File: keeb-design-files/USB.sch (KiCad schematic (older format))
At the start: 1 part

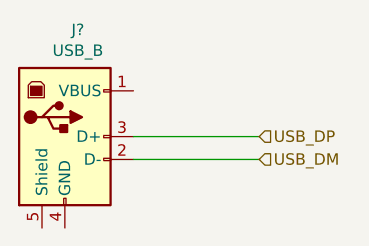
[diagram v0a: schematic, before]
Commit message: Add new Crystal and match symbols and footprints for switches and diodes
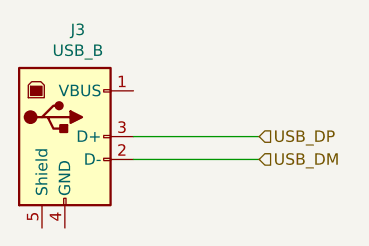
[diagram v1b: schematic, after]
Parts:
- gave numbers to parts that had none: 1
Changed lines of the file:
@@
 $Descr A4 11693 8268
 encoding utf-8
-Sheet 4 6
+Sheet 4 5
 Title "USB and Power Management"
 Date "2020-05-06"
@@
 $EndDescr
 $Comp
-L Connector:USB_B J?
+L Connector:USB_B J3
 U 1 1 5F00EB91
 P 1500 1950
-F 0 "J?" H 1557 2417 50  0000 C CNN
+F 0 "J3" H 1557 2417 50  0000 C CNN
 F 1 "USB_B" H 1557 2326 50  0000 C CNN
 F 2 "" H 1650 1900 50  0001 C CNN

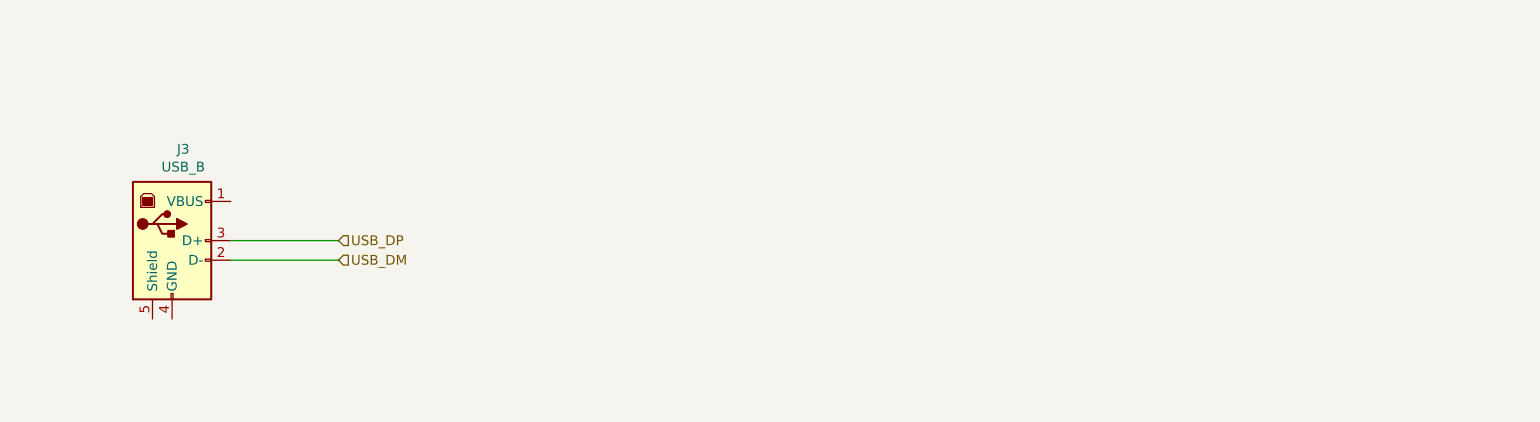
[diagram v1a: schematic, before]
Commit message: Add ESD diodes, USB isolator and LDO to schematic
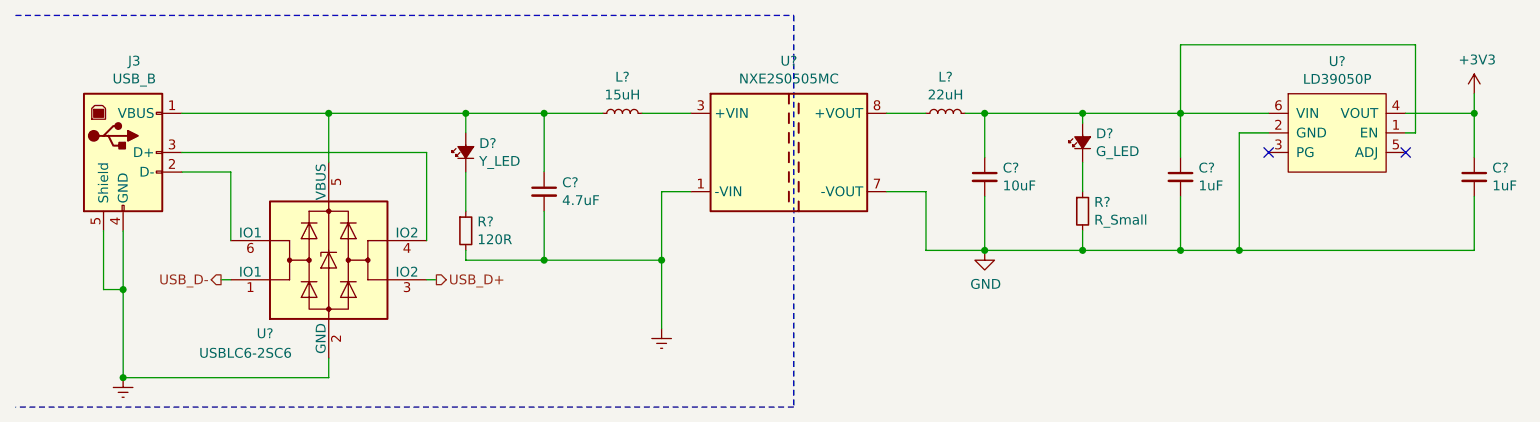
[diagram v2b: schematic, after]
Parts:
- added C?: 4.7uF, symbol Device:C_Small
- added C?: 10uF, symbol Device:C_Small
- added C? (x2): 1uF, symbol Device:C_Small
- added D?: Y_LED, symbol Device:LED_Small_ALT
- added D?: G_LED, symbol Device:LED_Small_ALT
- added L?: 15uH, symbol Device:L_Small
- added L?: 22uH, symbol Device:L_Small
- added R?: 120R, symbol Device:R_Small
- added R?: R_Small, symbol Device:R_Small
- added U?: NXE2S0505MC, Converter_DCDC:Converter_DCDC_muRata_NXE2SxxxxMC_THT, symbol Regulator_Switching:NXE2S0505MC
- added U?: USBLC6-2SC6, Package_TO_SOT_SMD:SOT-23-6, symbol Power_Protection:USBLC6-2SC6
- added U?: LD39050P, Package_DFN_QFN:DFN-6-1EP_3x3mm_P0.95mm_EP1.7x2.6mm, symbol LDO:LD39050P
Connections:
- net at J3.1 (VBUS): now also C?.1, D?.2 (A), L?.1, U?.5 (VBUS)
- net Earth: now reaches J3.4 (GND)
- net Earth: now also J3.5 (Shield), C?.2, R?.2, U?.1 (-VIN), U?.2 (GND)
- net USB_DM: no longer names the net of J3.2 (D-)
- net USB_DM: now also U?.6 (IO1)
- net USB_DP: no longer names the net of J3.3 (D+)
- net USB_DP: now also U?.4 (IO2)
- new net: L?.2, U?.3 (+VIN)
- new net: L?.1, U?.8 (+VOUT)
- new net: D?.1 (K), R?.1 (x2)
- new net: C?.1, C?.1, D?.2 (A), L?.2, U?.1 (EN), U?.6 (VIN)
- new net +3V3: C?.1, U?.4 (VOUT)
- new net GND: C?.2, C?.2, C?.2, R?.2, U?.2 (GND), U?.7 (-VOUT)
- new net USB_D+: U?.3 (IO2)
- new net USB_D-: U?.1 (IO1)
- no-connect marks 0 -> 2
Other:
- moved on the sheet: J3

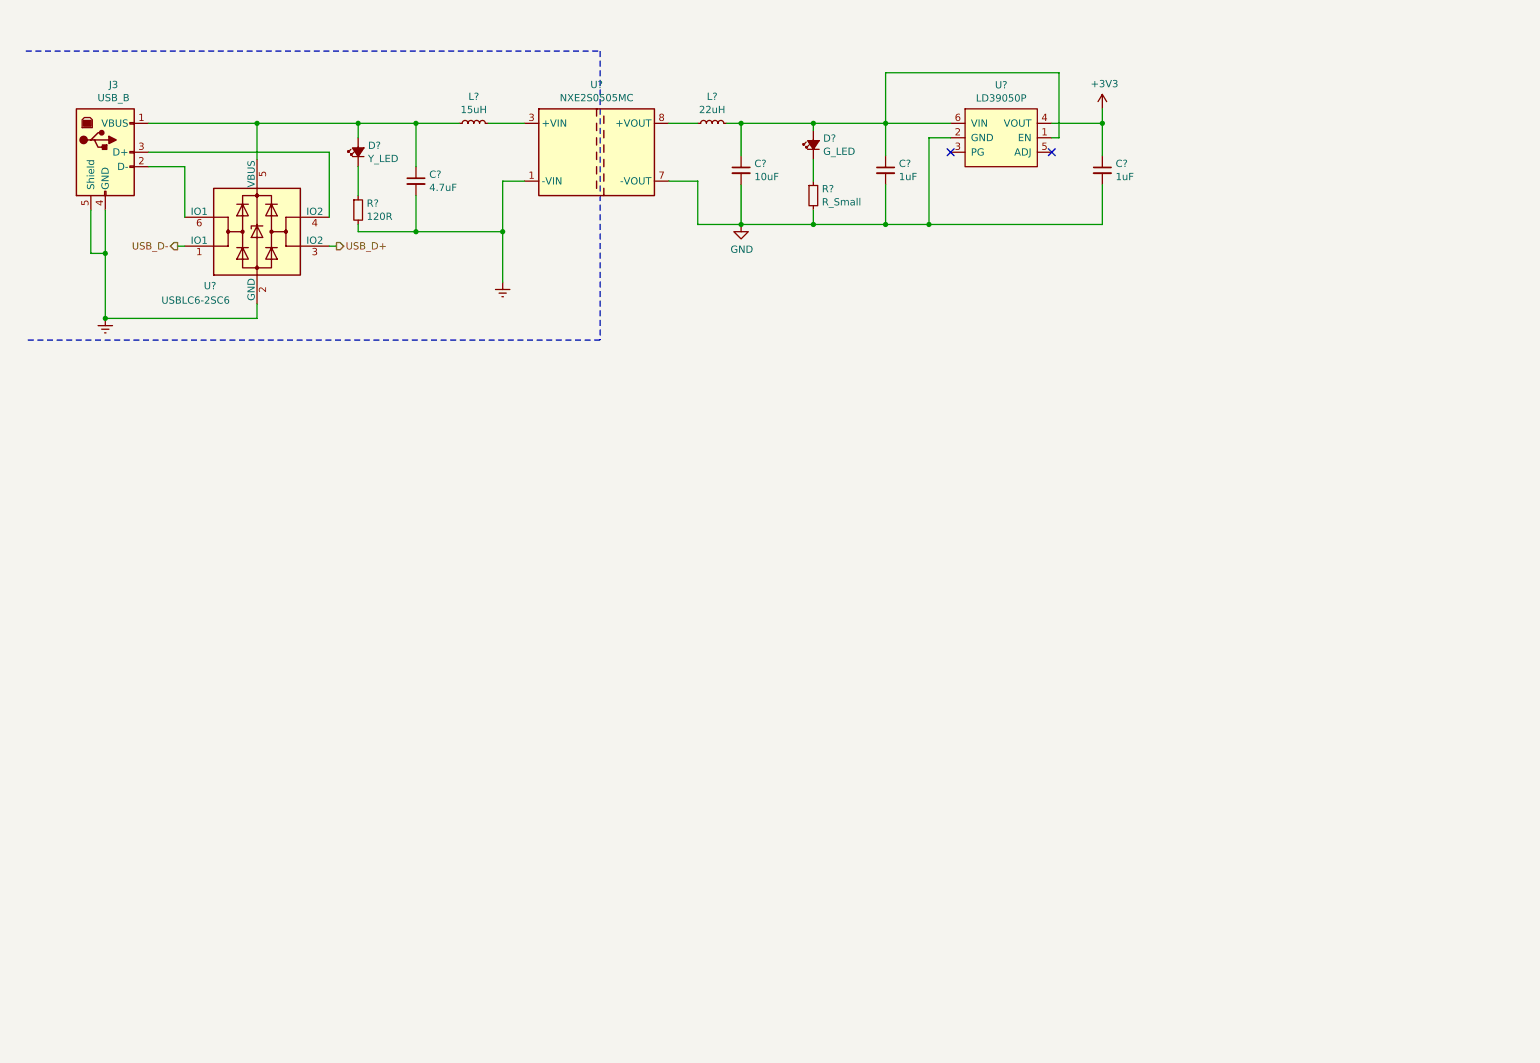
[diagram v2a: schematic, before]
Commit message: Start Battery Management and routed matrix to STM32L0
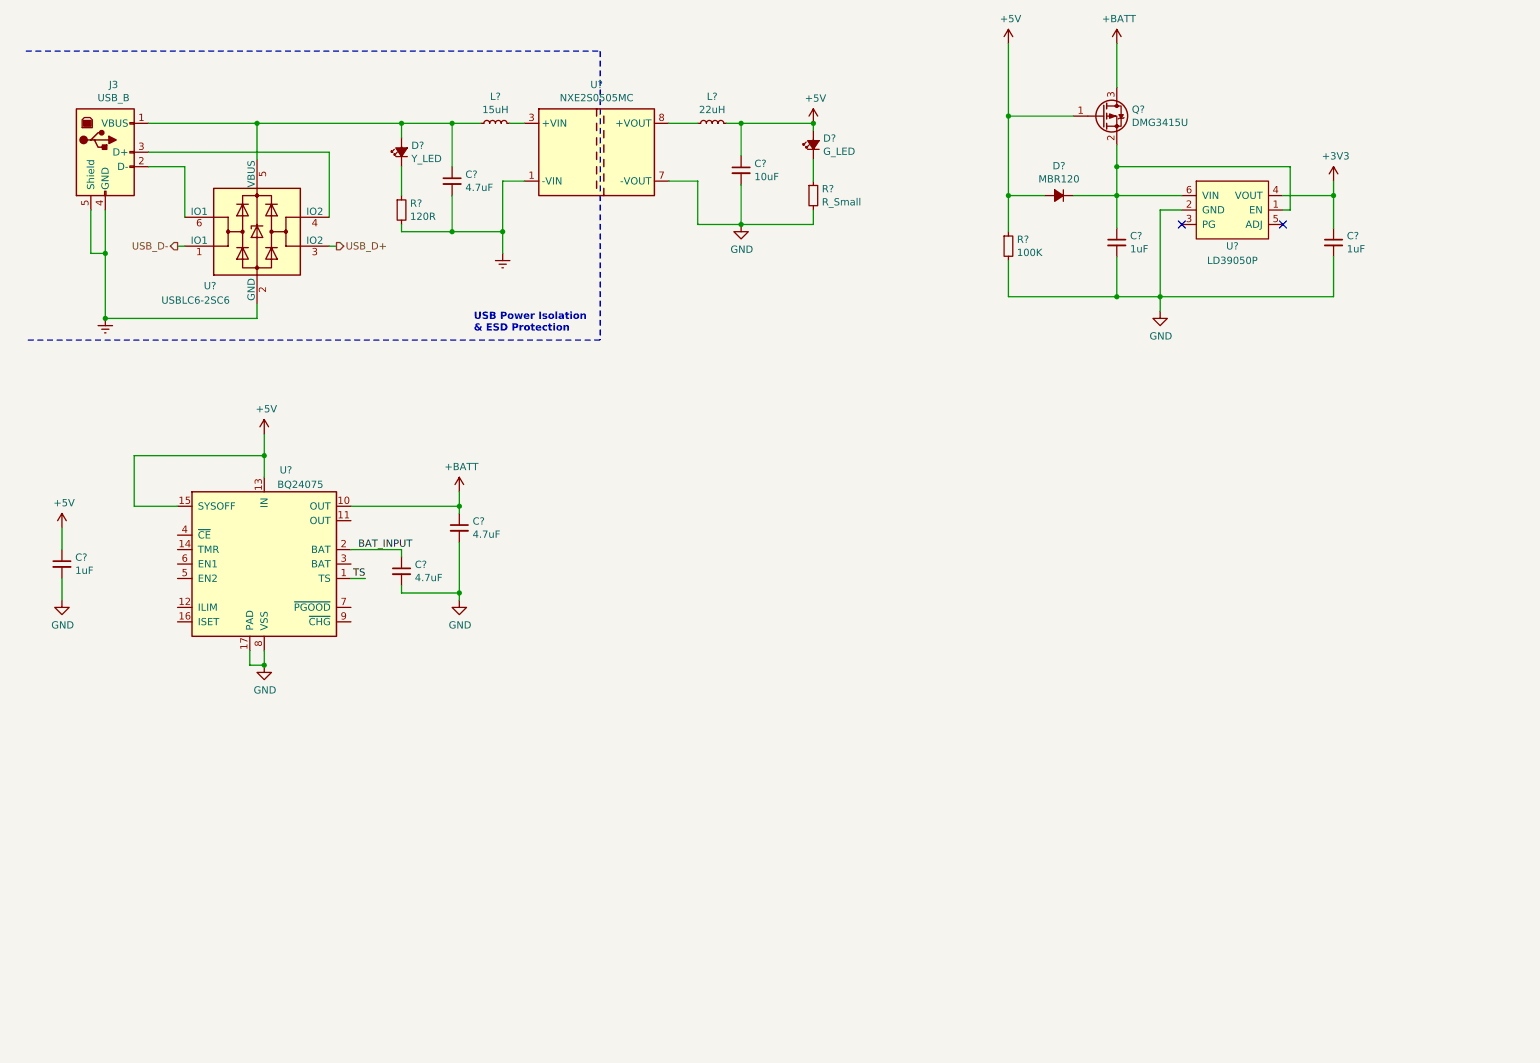
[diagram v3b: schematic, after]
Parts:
- added C?: 1uF, symbol Device:C_Small
- added C? (x2): 4.7uF, symbol Device:C_Small
- added D?: MBR120, Diode_SMD:D_SOD-123F, symbol Device:D_Small_ALT
- added Q?: DMG3415U, Package_TO_SOT_SMD:SOT-23, symbol Device:Q_PMOS_GSD
- added R?: 100K, symbol Device:R_Small
- added U?: BQ24075, symbol Battery_Management:BQ24075
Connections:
- net GND: now also C?.2, C?.2, C?.2, R?.2, U?.17 (PAD), U?.8 (VSS)
- net at C?.1, U?.1 (EN), U?.6 (VIN): now also D?.1 (K), Q?.2 (S); no longer C?.1, D?.2 (A), L?.2
- new net +5V: C?.1, C?.1, D?.2 (A), D?.2 (A), L?.2, Q?.1 (G), R?.1, U?.13 (IN), U?.15 (SYSOFF)
- new net +BATT: C?.1, Q?.3 (D), U?.10 (OUT)
- new net BAT_INPUT: C?.1, U?.2 (BAT)
- new net TS: U?.1 (TS)
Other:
- note added: "USB Power Isolation\n& ESD Protection"
- moved on the sheet: C?, D?, L?, R?, U?

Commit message: Add more part #'s, change to STM32L452CEUxx MCU, more layout work
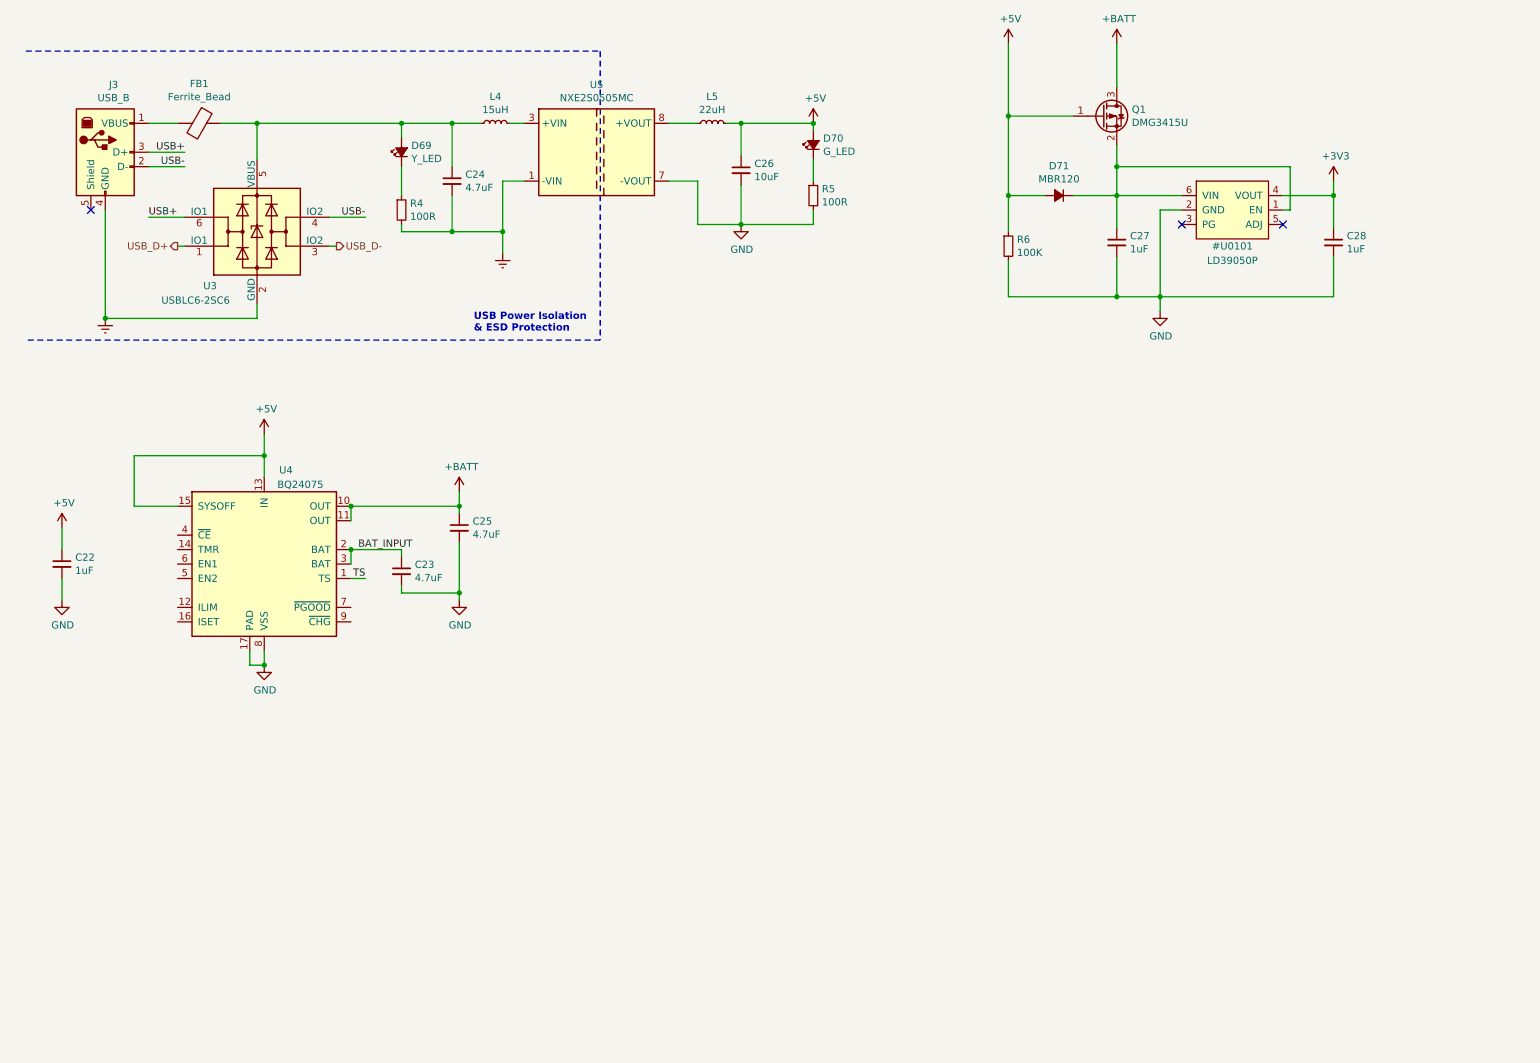
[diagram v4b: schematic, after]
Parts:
- removed U?: LD39050P, Package_DFN_QFN:DFN-6-1EP_3x3mm_P0.95mm_EP1.7x2.6mm, symbol LDO:LD39050P
- added FB1: Ferrite_Bead, symbol Device:Ferrite_Bead
- C23, C24, C25: renamed from C?; footprint (none) -> Capacitor_SMD:C_0603_1608Metric; LCSC Part Number (none) -> C19666
- C26: renamed from C?; footprint (none) -> Capacitor_SMD:C_0603_1608Metric; LCSC Part Number (none) -> C19702
- D69, D70: renamed from D?; footprint (none) -> LED_SMD:LED_0603_1608Metric
- J3: footprint (none) -> lib_fp:USB-B1HSW6
- L5: renamed from L?; LCSC Part Number (none) -> C132137
- R4: renamed from R?; value 120R -> 100R; footprint (none) -> Resistor_SMD:R_0402_1005Metric; LCSC Part Number (none) -> C25741
- R5: renamed from R?; value R_Small -> 100R; footprint (none) -> Resistor_SMD:R_0402_1005Metric; LCSC Part Number (none) -> C25741
- R6: renamed from R?; footprint (none) -> Resistor_SMD:R_0402_1005Metric
- U4: renamed from U?; footprint (none) -> Package_DFN_QFN:QFN-16-1EP_3x3mm_P0.5mm_EP1.7x1.7mm
- gave numbers to parts that had none: 8
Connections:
- net +BATT: now also U4.11 (OUT)
- net BAT_INPUT: now also U4.3 (BAT)
- net Earth: no longer J3.5 (Shield)
- net USB_D+: now also U3.1 (IO1); no longer U3.3 (IO2)
- net USB_D-: now also U3.3 (IO2); no longer U3.1 (IO1)
- net USB+: now reaches J3.3 (D+)
- net USB+: now also U3.6 (IO1); no longer U3.4 (IO2)
- net at C24.1, D69.2 (A), L4.1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: now also FB1.1; no longer J3.1 (VBUS)
- net USB-: now reaches J3.2 (D-)
- net USB-: now also U3.4 (IO2); no longer U3.6 (IO1)
- new net: FB1.2, J3.1 (VBUS)
- no-connect marks 2 -> 3

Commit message: Add Battery Input, Thermistor Input, and SYSOFF Switch
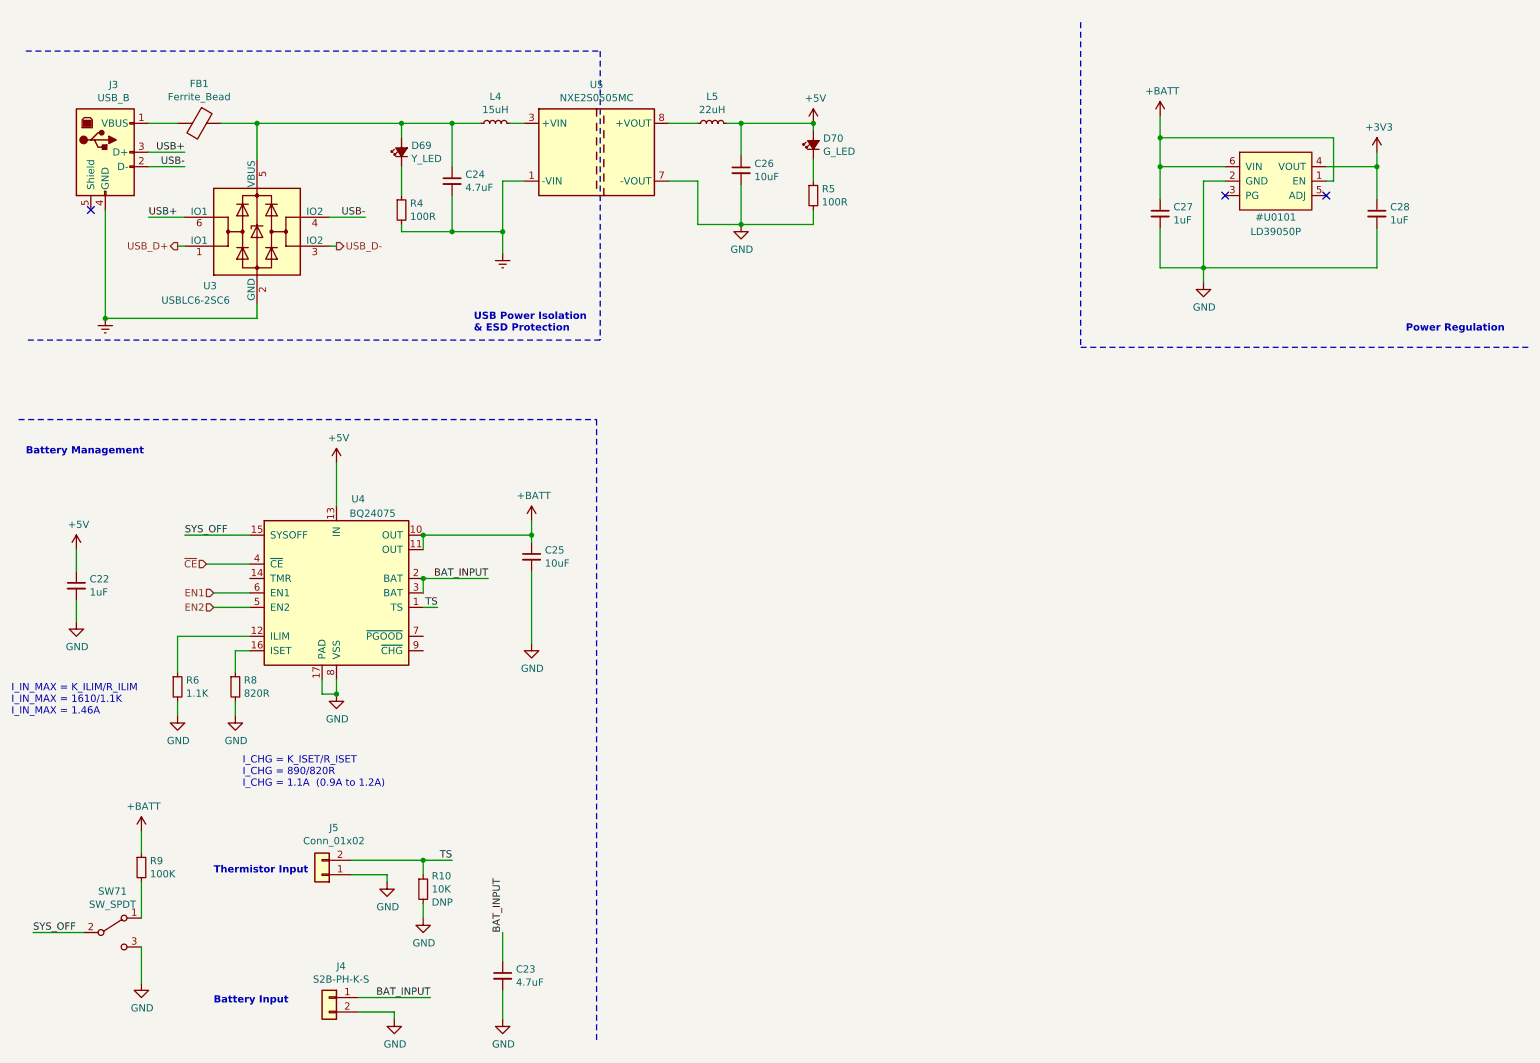
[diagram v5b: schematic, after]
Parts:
- removed D71: MBR120, Diode_SMD:D_SOD-123F, symbol Device:D_Small_ALT
- removed Q1: DMG3415U, Package_TO_SOT_SMD:SOT-23, symbol Device:Q_PMOS_GSD
- added J4: S2B-PH-K-S, Connector_JST:JST_PH_S2B-PH-K_1x02_P2.00mm_Horizontal, symbol Connector_Generic:Conn_01x02
- added J5: Conn_01x02, Connector_JST:JST_PH_S2B-PH-K_1x02_P2.00mm_Horizontal, symbol Connector_Generic:Conn_01x02
- added R10: 10K, symbol Device:R_Small
- added R8: 820R, symbol Device:R_Small
- added R9: 100K, symbol Device:R_Small
- added SW71: SW_SPDT, lib_fp:SW_CuK_OS102011MA1QN1_SPDT_Angled, symbol Switch:SW_SPDT
- C25: value 4.7uF -> 10uF; LCSC Part Number C19666 -> C19702
- R6: value 100K -> 1.1K; footprint Resistor_SMD:R_0402_1005Metric -> (none); LCSC Part Number (none) -> C25860
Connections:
- net +5V: no longer R6.1, U4.15 (SYSOFF)
- net +BATT: now also C27.1, R9.1
- net BAT_INPUT: now also J4.1 (Pin_1)
- net GND: now also J4.2 (Pin_2), J5.1 (Pin_1), R10.2, R8.2, SW71.3 (C)
- net TS: now also J5.2 (Pin_2), R10.1
- net at U4.12 (ILIM): now also R6.1
- net at U4.16 (ISET): now also R8.1
- net ~CE~: now reaches U4.4 (~CE)
- net EN2: now reaches U4.5 (EN2)
- net EN1: now reaches U4.6 (EN1)
- new net: R9.2, SW71.1 (A)
- new net SYS_OFF: SW71.2 (B), U4.15 (SYSOFF)
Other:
- note added: "Battery Input"
- note added: "Battery Management"
- note added: "I_CHG = K_ISET/R_ISET\nI_CHG = 890/820R\nI_CHG = 1.1A (0.9A to 1.2A)"
- note added: "I_IN_MAX = K_ILIM/R_ILIM\nI_IN_MAX = 1610/1.1K\nI_IN_MAX = 1.46A"
- note added: "Power Regulation"
- note added: "Thermistor Input"
- moved on the sheet: C22, C23, C25, C27, C28, U4
